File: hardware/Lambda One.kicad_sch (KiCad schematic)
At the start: 24 parts, among them IC1 DS1818, J1 Conn_01x02, SW1 SW_Push, U1 W65C816SxP, U12 74HC245, U3 ATF22LV10C, U8 74HC00, U9 74HC00, Y1 TFT680

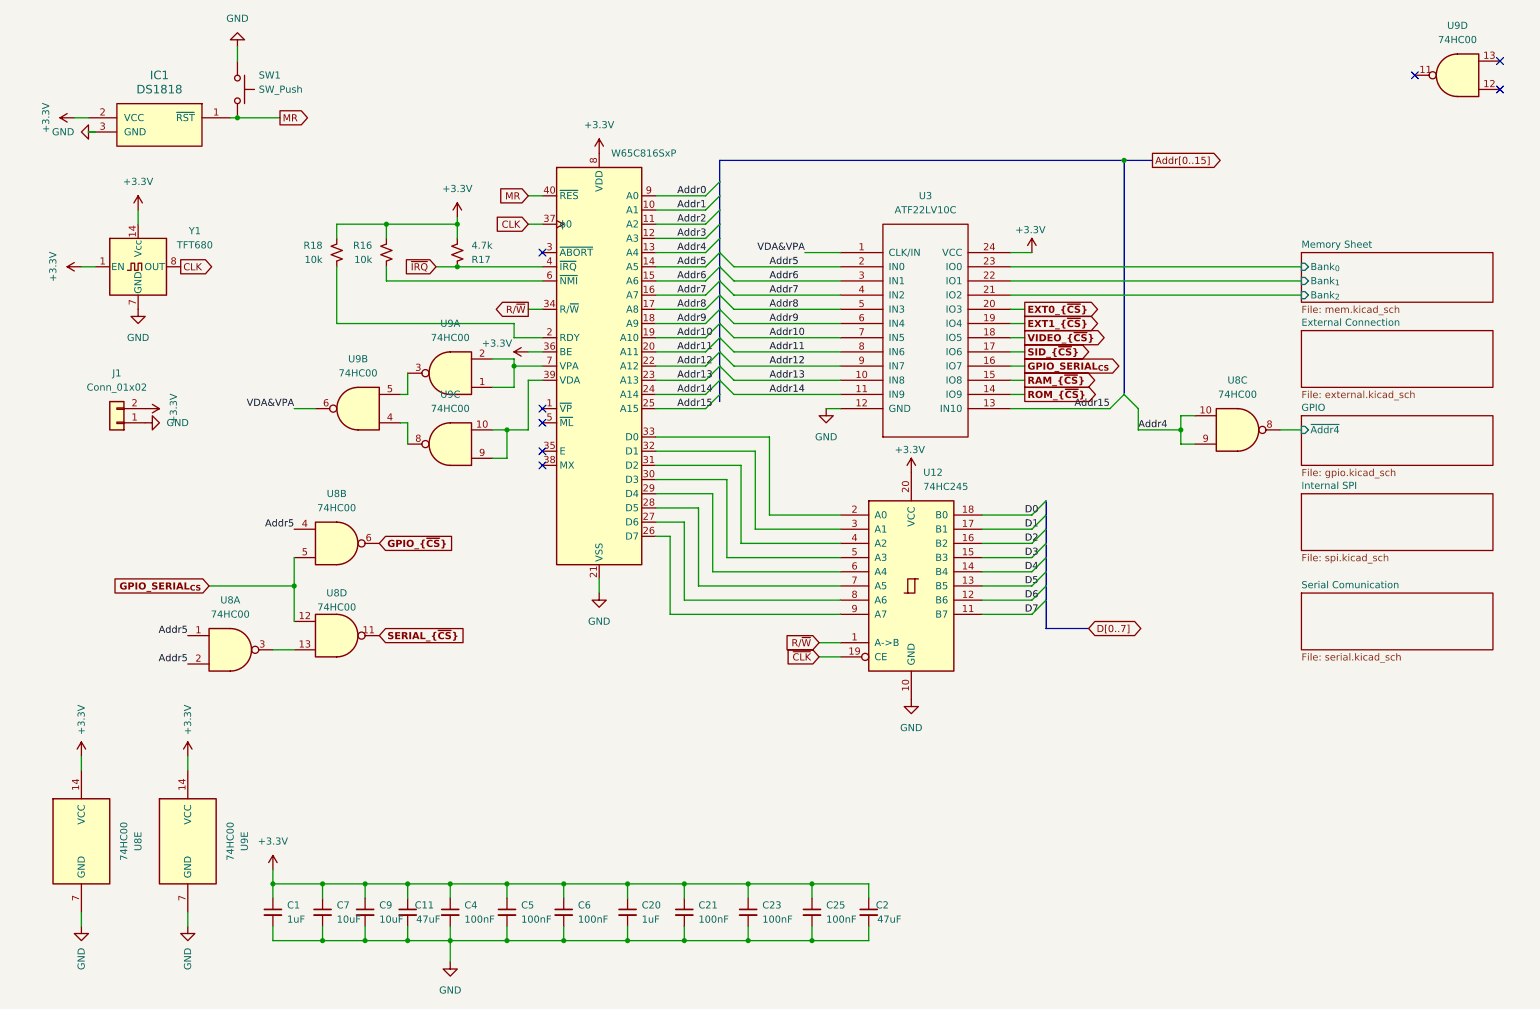
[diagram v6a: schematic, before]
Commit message: IMproved Serial With New CHIP, IMproved Video, Added external Serial Connections
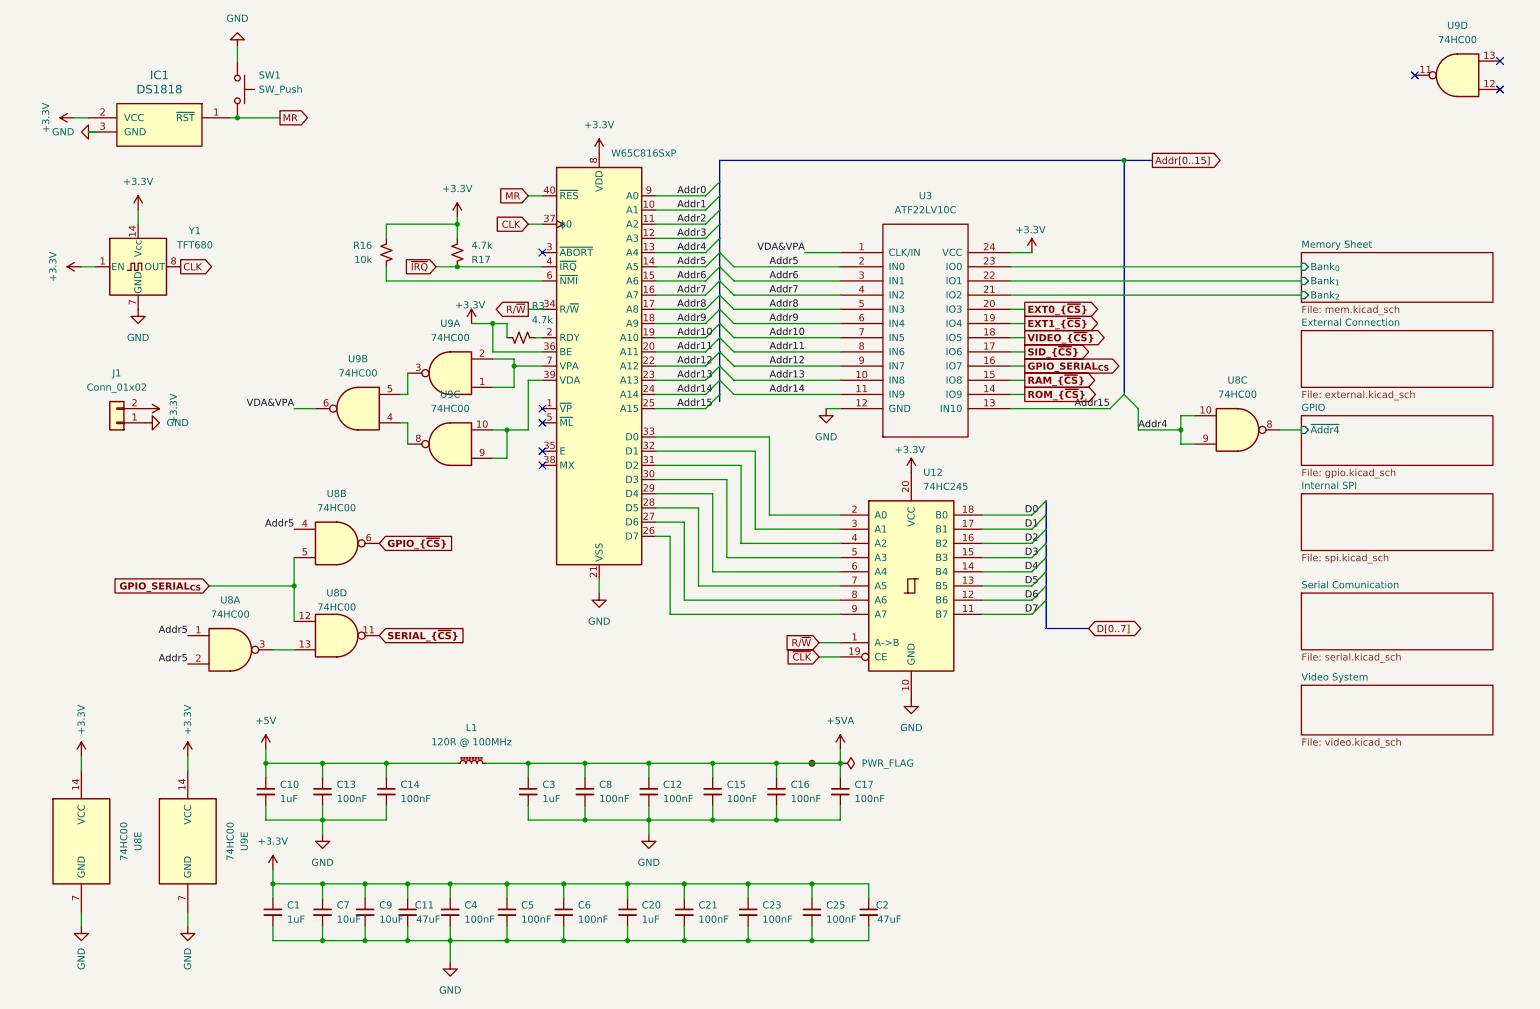
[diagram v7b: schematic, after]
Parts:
- removed R18: 10k, Resistor_SMD:R_0603_1608Metric, symbol Device:R_Small_US
- added C10, C3: 1uF, Capacitor_SMD:C_0603_1608Metric, symbol Device:C_Small
- added C12, C13, C14, C15, C16, C17, C8: 100nF, Capacitor_SMD:C_0603_1608Metric, symbol Device:C_Small
- added L1: 120R @ 100MHz, Inductor_SMD:L_0603_1608Metric, symbol Device:L_Ferrite_Small
- added R3: 4.7k, Resistor_SMD:R_0603_1608Metric, symbol Device:R_Small_US
- added TP1: TestPoint_Small, TestPoint:TestPoint_Pad_D1.5mm, symbol Connector:TestPoint_Small
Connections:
- net +3.3V: now also R3.2
- net GND: now also C10.2, C12.2, C13.2, C14.2, C15.2, C16.2, C17.2, C3.2, C8.2
- net at U1.2 (RDY): now also R3.1
- new net +5V: C10.1, C13.1, C14.1, L1.1
- new net +5VA: C12.1, C15.1, C16.1, C17.1, C3.1, C8.1, L1.2, TP1.1
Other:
- added sheet Video System (video.kicad_sch)

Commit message: Minor Improvemnts
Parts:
- U8, U9: footprint (none) -> Package_DIP:DIP-14_W7.62mm
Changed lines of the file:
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@@
 			)
 		)
-		(property "Footprint" ""
+		(property "Footprint" "Package_DIP:DIP-14_W7.62mm"
 			(at 88.9 95.25 0)
 			(effects
@@
 			)
 		)
-		(property "Footprint" ""
+		(property "Footprint" "Package_DIP:DIP-14_W7.62mm"
 			(at 68.58 129.54 0)
 			(effects
@@
 			)
 		)
-		(property "Footprint" ""
+		(property "Footprint" "Package_DIP:DIP-14_W7.62mm"
 			(at 88.9 82.55 0)
 			(effects
@@
 			)
 		)
-		(property "Footprint" ""
+		(property "Footprint" "Package_DIP:DIP-14_W7.62mm"
 			(at 68.58 113.03 0)
 			(effects
@@
 			)
 		)
-		(property "Footprint" ""
+		(property "Footprint" "Package_DIP:DIP-14_W7.62mm"
 			(at 269.24 29.21 0)
 			(effects
@@
 			)
 		)
-		(property "Footprint" ""
+		(property "Footprint" "Package_DIP:DIP-14_W7.62mm"
 			(at 22.86 166.37 0)
 			(effects
@@
 			)
 		)
-		(property "Footprint" ""
+		(property "Footprint" "Package_DIP:DIP-14_W7.62mm"
 			(at 229.87 92.71 0)
 			(effects
@@
 			)
 		)
-		(property "Footprint" ""
+		(property "Footprint" "Package_DIP:DIP-14_W7.62mm"
 			(at 72.39 88.9 0)
 			(effects
@@
 			)
 		)
-		(property "Footprint" ""
+		(property "Footprint" "Package_DIP:DIP-14_W7.62mm"
 			(at 49.53 132.08 0)
 			(effects
@@
 			)
 		)
-		(property "Footprint" ""
+		(property "Footprint" "Package_DIP:DIP-14_W7.62mm"
 			(at 41.91 166.37 0)
 			(effects
